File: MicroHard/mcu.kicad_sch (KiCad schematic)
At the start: 28 parts, among them J2 GPIO_header, J3 MCU_Debug, J4 Micro_SD_Card_Det2, J5 Controller Connector, SW1 KMR221NGLFS, SW2 KMR221NGLFS, SW3 KMR221NGLFS, U3 EFM32GG842F1024, Y1 48MHz

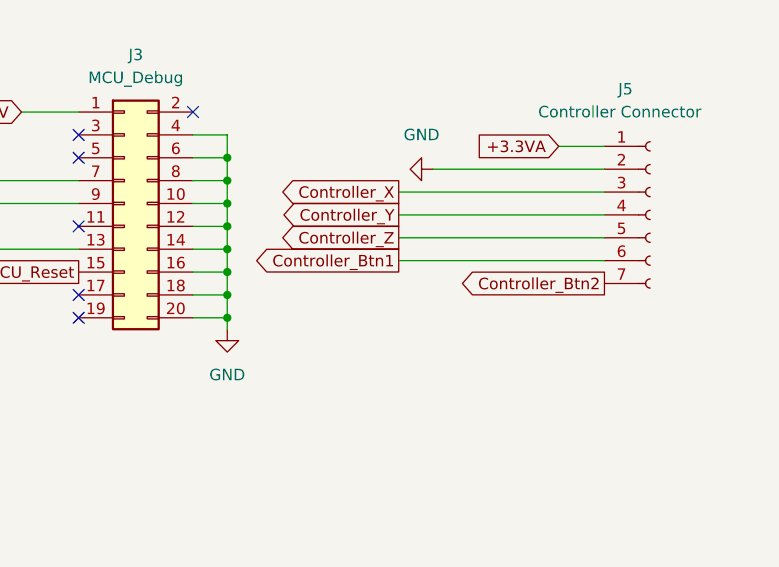
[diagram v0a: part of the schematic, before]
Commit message: added VGA footprint
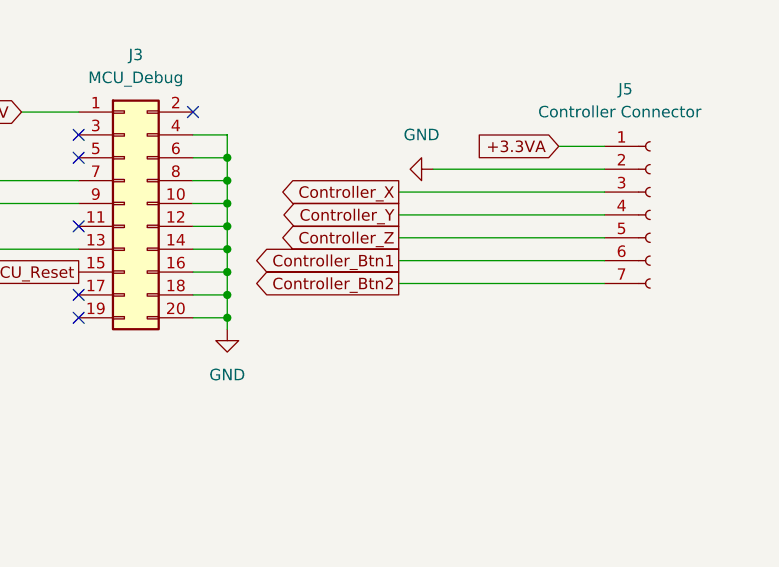
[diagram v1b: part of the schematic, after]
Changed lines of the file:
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@@
 	(wire
 		(pts
+			(xy 238.76 114.3) (xy 261.62 114.3)
+		)
+		(stroke
+			(width 0)
+			(type default)
+		)
+	)
+	(wire
+		(pts
 			(xy 105.41 36.83) (xy 99.06 36.83)
 		)
@@
 	(global_label "Controller_Btn2"
 		(shape output)
-		(at 261.62 114.3 180)
+		(at 238.76 114.3 180)
 		(fields_autoplaced yes)
 		(effects
@@
 		)
 		(property "Intersheetrefs" "${INTERSHEET_REFS}"
-			(at 243.8789 114.3 0)
+			(at 221.0189 114.3 0)
 			(effects
 				(font

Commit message: Initial layout
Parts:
- renumbered C27 to C20, C28 to C21, C25 to C24, C29 to C25, C30 to C26, C31 to C27, C20 to C28, C21 to C29, C24 to C30, C26 to C31, J4 to J2, J2 to J3, J3 to J4, R14 to R11, R15 to R13, R13 to R14, R11 to R15

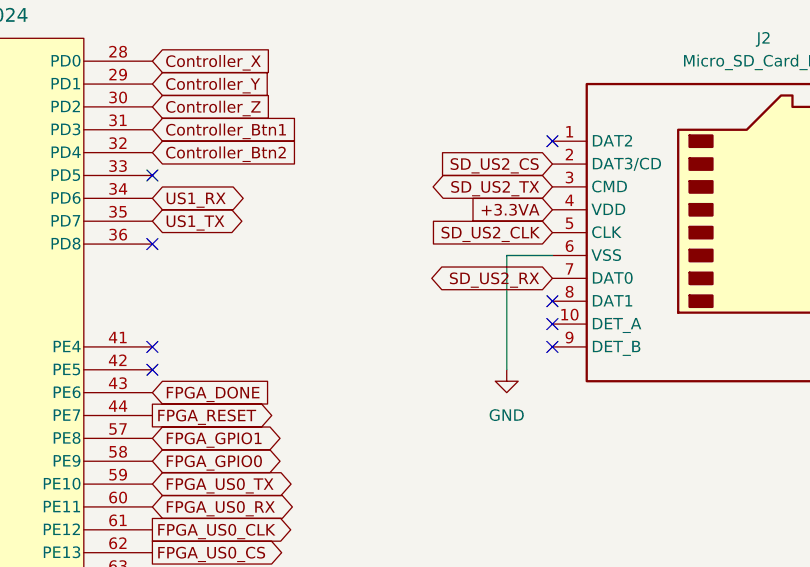
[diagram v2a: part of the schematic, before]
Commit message: power plane
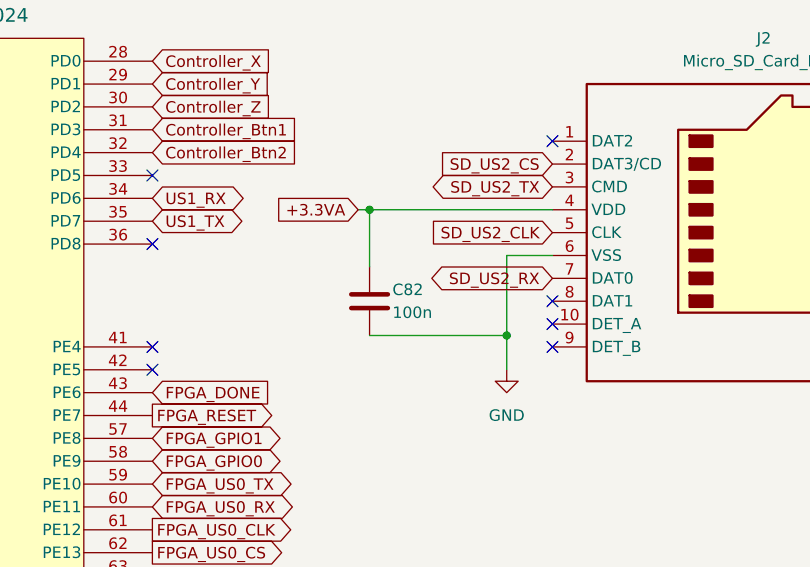
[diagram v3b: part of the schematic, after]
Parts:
- added C82: 100n, Capacitor_SMD:C_1206_3216Metric_Pad1.33x1.80mm_HandSolder, symbol Device:C
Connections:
- net +3.3VA: now also C82.1
- net GND: now also C82.2
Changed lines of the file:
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@@
 	)
 	(junction
+		(at 214.63 59.69)
+		(diameter 0)
+		(color 0 0 0 0)
+	)
+	(junction
+		(at 199.39 45.72)
+		(diameter 0)
+		(color 0 0 0 0)
+	)
+	(junction
 		(at 219.71 100.33)
 		(diameter 0)
@@
 	(wire
 		(pts
+			(xy 199.39 59.69) (xy 214.63 59.69)
+		)
+		(stroke
+			(width 0)
+			(type default)
+		)
+	)
+	(wire
+		(pts
 			(xy 139.7 170.18) (xy 133.35 170.18)
 		)
@@
 	(wire
 		(pts
+			(xy 199.39 45.72) (xy 199.39 52.07)
+		)
+		(stroke
+			(width 0)
+			(type default)
+		)
+	)
+	(wire
+		(pts
 			(xy 215.9 105.41) (xy 219.71 105.41)
 		)
@@
 	(wire
 		(pts
+			(xy 198.12 45.72) (xy 199.39 45.72)
+		)
+		(stroke
+			(width 0)
+			(type default)
+		)
+	)
+	(wire
+		(pts
 			(xy 133.35 160.02) (xy 146.05 160.02)
 		)
@@
 	(wire
 		(pts
+			(xy 199.39 45.72) (xy 219.71 45.72)
+		)
+		(stroke
+			(width 0)
+			(type default)
+		)
+	)
+	(wire
+		(pts
 			(xy 193.04 100.33) (xy 193.04 105.41)
 		)
@@
 	(wire
 		(pts
+			(xy 214.63 59.69) (xy 214.63 63.5)
+		)
+		(stroke
+			(width 0)
+			(type default)
+		)
+	)
+	(wire
+		(pts
 			(xy 133.35 167.64) (xy 133.35 170.18)
 		)
@@
 	(wire
 		(pts
-			(xy 214.63 50.8) (xy 214.63 63.5)
+			(xy 214.63 50.8) (xy 214.63 59.69)
 		)
 		(stroke
@@
 	(global_label "+3.3VA"
 		(shape input)
-		(at 219.71 45.72 180)
+		(at 198.12 45.72 180)
 		(fields_autoplaced yes)
 		(effects
@@
 		)
 		(property "Intersheetrefs" "${INTERSHEET_REFS}"
-			(at 209.9514 45.72 0)
+			(at 188.3614 45.72 0)
 			(effects
 				(font
@@
 					(unit 1)
 				)
+			)
+		)
+	)
+	(symbol
+		(lib_id "Device:C")
+		(at 199.39 55.88 0)
+		(unit 1)
+		(exclude_from_sim no)
+		(in_bom yes)
+		(on_board yes)
+		(dnp no)
+		(property "Reference" "C82"
+			(at 201.93 54.61 0)
+			(effects
+				(font
+					(size 1.27 1.27)
+				)
+				(justify left)
+			)
+		)
+		(property "Value" "100n"
+			(at 201.93 57.15 0)
+			(effects
+				(font
+					(size 1.27 1.27)
+				)
+				(justify left)
+			)
+		)
+		(property "Footprint" "Capacitor_SMD:C_1206_3216Metric_Pad1.33x1.80mm_HandSolder"
+			(at 200.3552 59.69 0)
+			(effects
+				(font
+					(size 1.27 1.27)
+				)
+				(hide yes)
+			)
+		)
+		(property "Datasheet" "~"
+			(at 199.39 55.88 0)
+			(effects
+				(font
+					(size 1.27 1.27)
+				)
+				(hide yes)
+			)
+		)
+		(property "Description" "Unpolarized capacitor"
+			(at 199.39 55.88 0)
+			(effects
+				(font
+					(size 1.27 1.27)
+				)
+				(hide yes)
+			)
+		)
+		(pin "2"
+		)
+		(pin "1"
+		)
+		(instances
+			(project ""
+				(path "/578bd531-a491-4b15-a479-460d159ffc14/51bb8540-90e7-4b9a-973c-776e3825d084"
+					(reference "C82")
+					(unit 1)
+				)

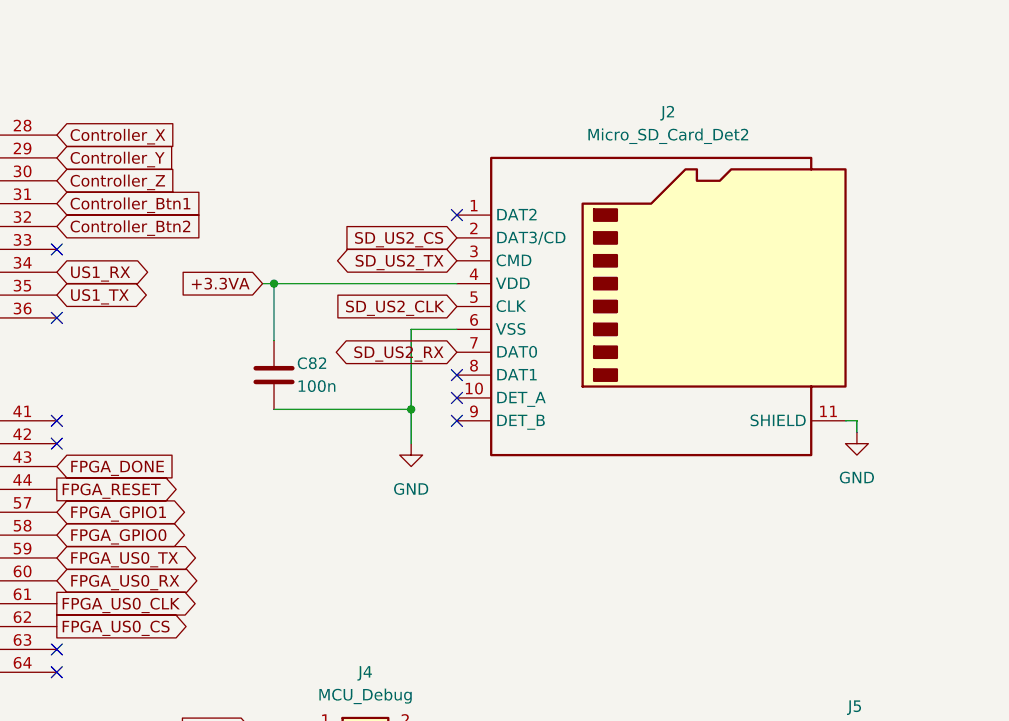
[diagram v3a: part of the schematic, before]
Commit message: Power supply layout
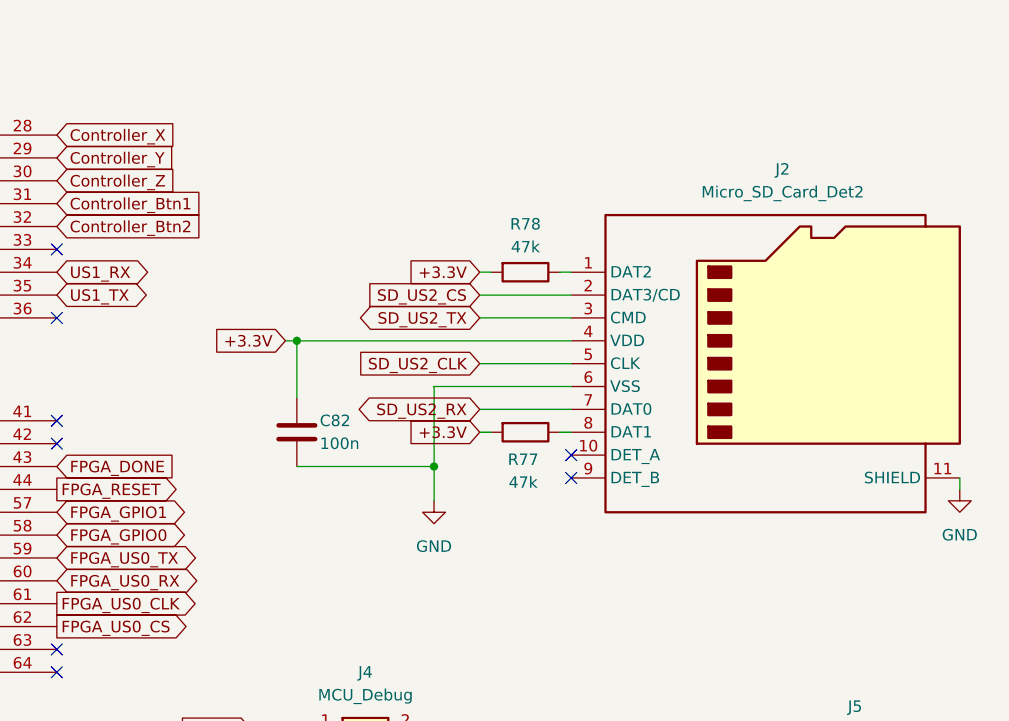
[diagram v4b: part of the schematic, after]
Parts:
- added R77, R78: 47k, Resistor_SMD:R_1206_3216Metric_Pad1.30x1.75mm_HandSolder, symbol Device:R
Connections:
- net +3.3V: now also C82.1, J2.4 (VDD), R77.2, R78.2
- net +3.3VA: no longer C82.1, J2.4 (VDD)
- net at J2.1 (DAT2): now also R78.1
- net at J2.8 (DAT1): now also R77.1
- no-connect marks 30 -> 28
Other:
- moved on the sheet: C82, J2

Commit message: Final changes
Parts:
- J4: footprint Connector_PinHeader_1.00mm:PinHeader_2x10_P1.00mm_Vertical -> Connector_IDC:IDC-Header_2x10_P2.54mm_Vertical
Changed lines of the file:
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@@
 			)
 		)
-		(property "Footprint" "Connector_PinHeader_1.00mm:PinHeader_2x10_P1.00mm_Vertical"
+		(property "Footprint" "Connector_IDC:IDC-Header_2x10_P2.54mm_Vertical"
 			(at 208.28 105.41 0)
 			(effects

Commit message: Fix schematics for delivery
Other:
- company: (none) -> MicroHard
- title: Microcontroller unit -> Microcontroller unit (MCU)
